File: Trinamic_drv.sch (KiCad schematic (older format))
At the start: 5 parts

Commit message: Added FET Drivers + PNs. Started Trinamic drivers
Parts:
- added C? (x2): C, symbol Device:C
- added J? (x2): Conn_01x02, bountiful_harvest:MOLEX_1510481206_6.55p, symbol Connector_Generic:Conn_01x02
- added R? (x2): R, symbol Device:R
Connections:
- net labels added: +VDC, GND
- net labels removed: +24V
- wire segments 13 -> 37
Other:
- note added: "CLOSE TO PIN 31 AND 16"
- moved on the sheet: C?, U?

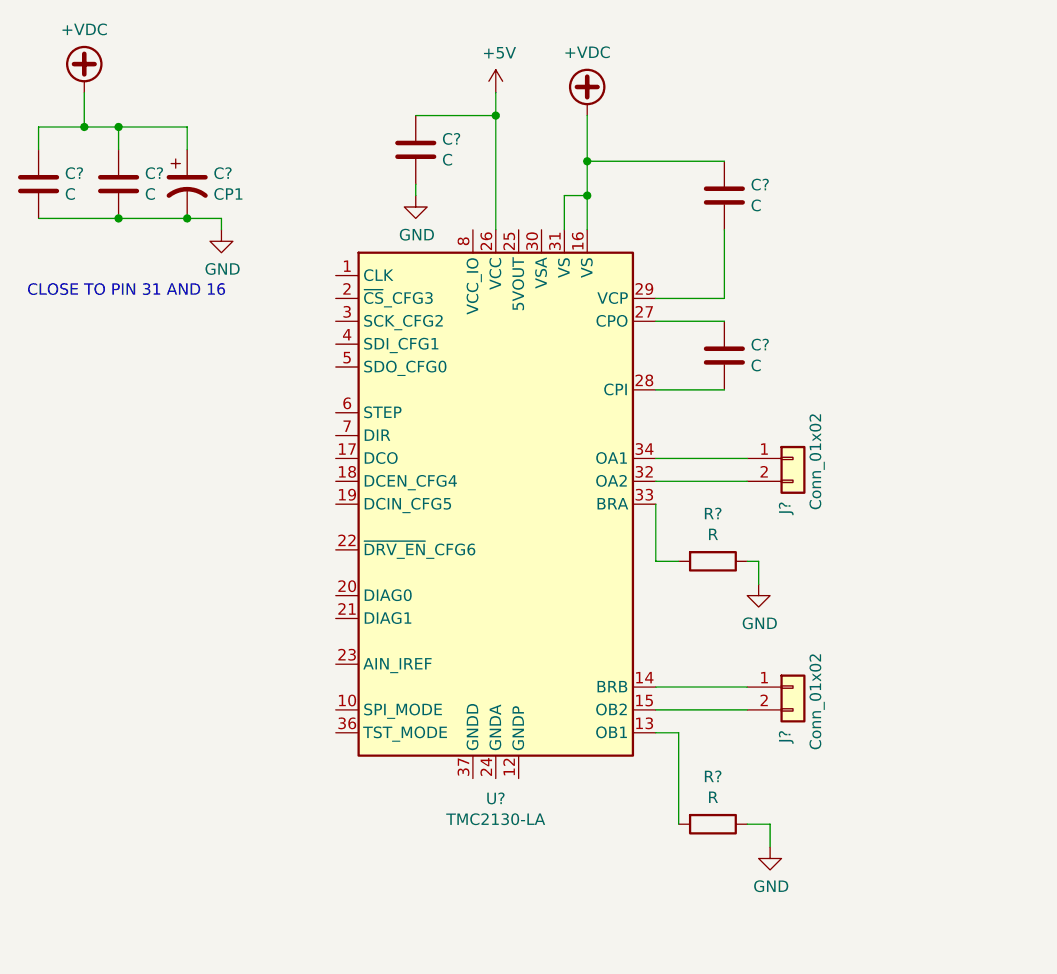
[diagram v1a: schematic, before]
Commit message: added SPI and sense resistors to stepper driver
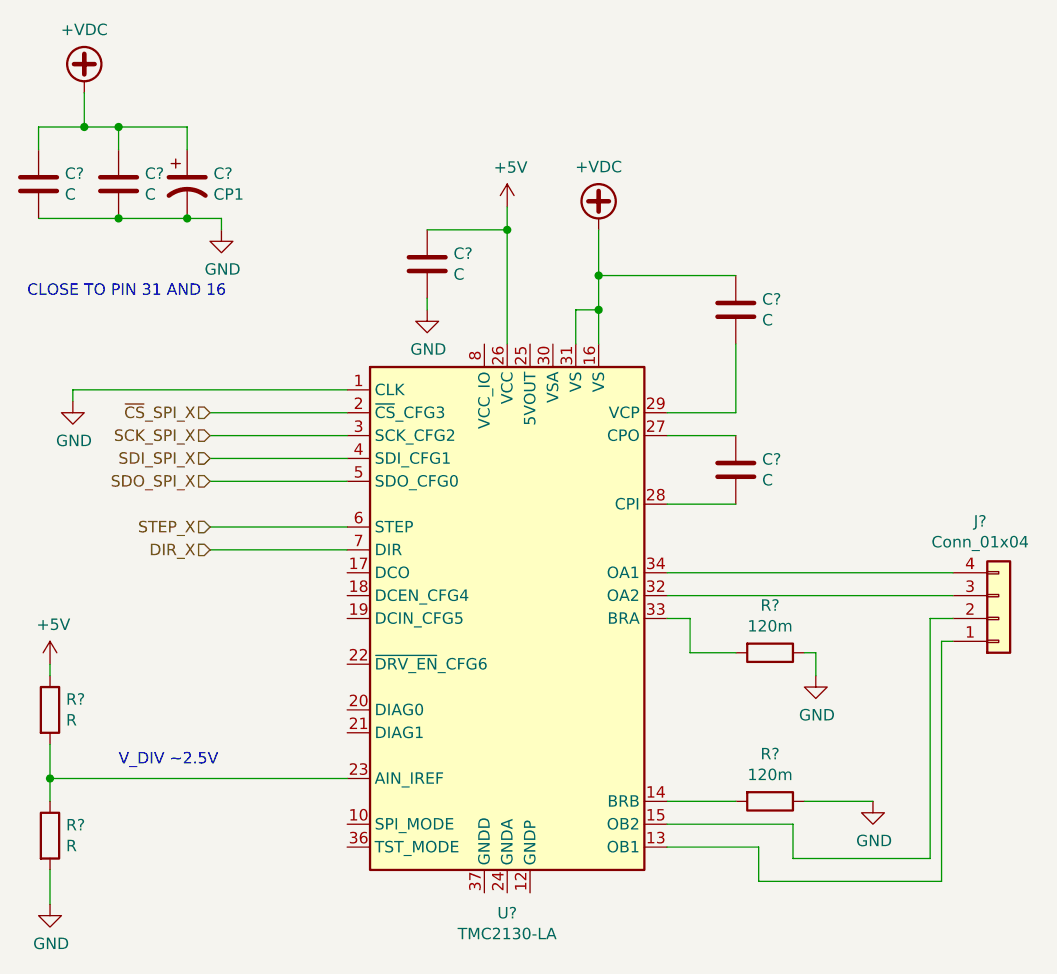
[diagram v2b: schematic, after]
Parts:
- removed J? (x2): Conn_01x02, bountiful_harvest:MOLEX_1510481206_6.55p, symbol Connector_Generic:Conn_01x02
- removed R?: R, symbol Device:R
- added J?: Conn_01x04, symbol Connector_Generic:Conn_01x04
- added R? (x2): R, symbol Device:R
- added R?: 120m, Resistors_SMD:R_2512_HandSoldering, symbol Device:R
- R?: value R -> 120m; footprint (none) -> Resistors_SMD:R_2512_HandSoldering; Manufacturer (none) -> Yageo; Vendor (none) -> Digi-Key; Vendor P/N (none) -> 311-0.12TCT-ND
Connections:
- net +5V: now also R?.1
- net GND: now also U?.1 (CLK), R?.1, R?.2
- net at U?.13 (OB1): now also J?.1 (Pin_1)
- net at U?.14 (BRB): now also R?.2
- net at U?.15 (OB2): now also J?.2 (Pin_2)
- net ~CS~_SPI_X: now reaches U?.2 (~CS~_CFG3)
- net at U?.23 (AIN_IREF): now also R?.1, R?.2
- net SCK_SPI_X: now reaches U?.3 (SCK_CFG2)
- net at U?.32 (OA2): now also J?.3 (Pin_3)
- net at U?.34 (OA1): now also J?.4 (Pin_4)
- net SDI_SPI_X: now reaches U?.4 (SDI_CFG1)
- net SDO_SPI_X: now reaches U?.5 (SDO_CFG0)
- net STEP_X: now reaches U?.6 (STEP)
- net DIR_X: now reaches U?.7 (DIR)
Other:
- note added: "V_DIV ~~2.5V"
- moved on the sheet: C?, R?, U?

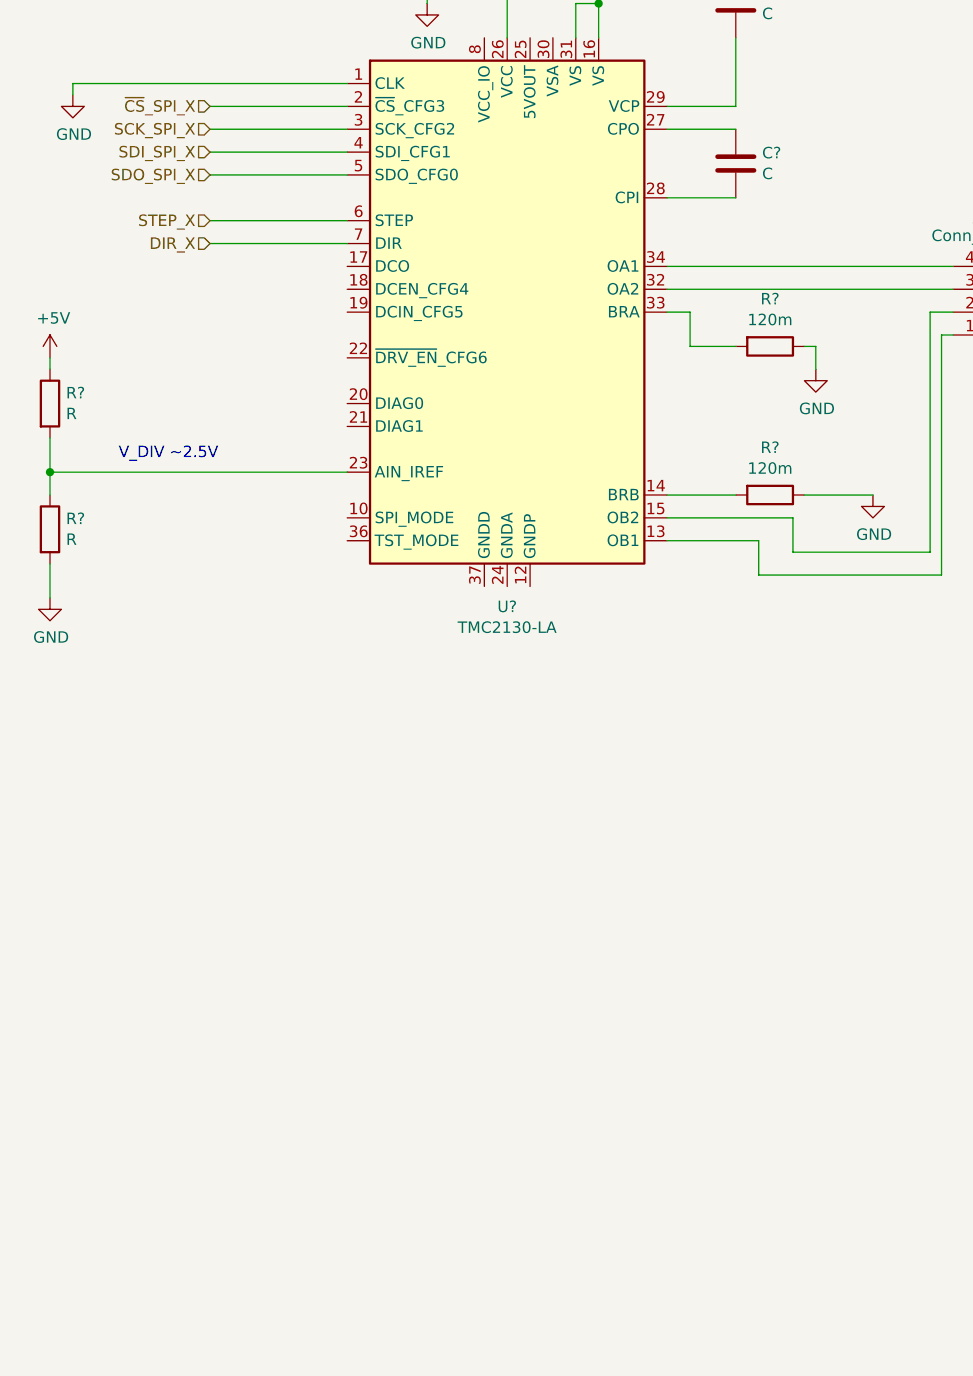
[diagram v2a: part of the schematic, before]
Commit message: Adding charge pump caps, SPI select, test mode
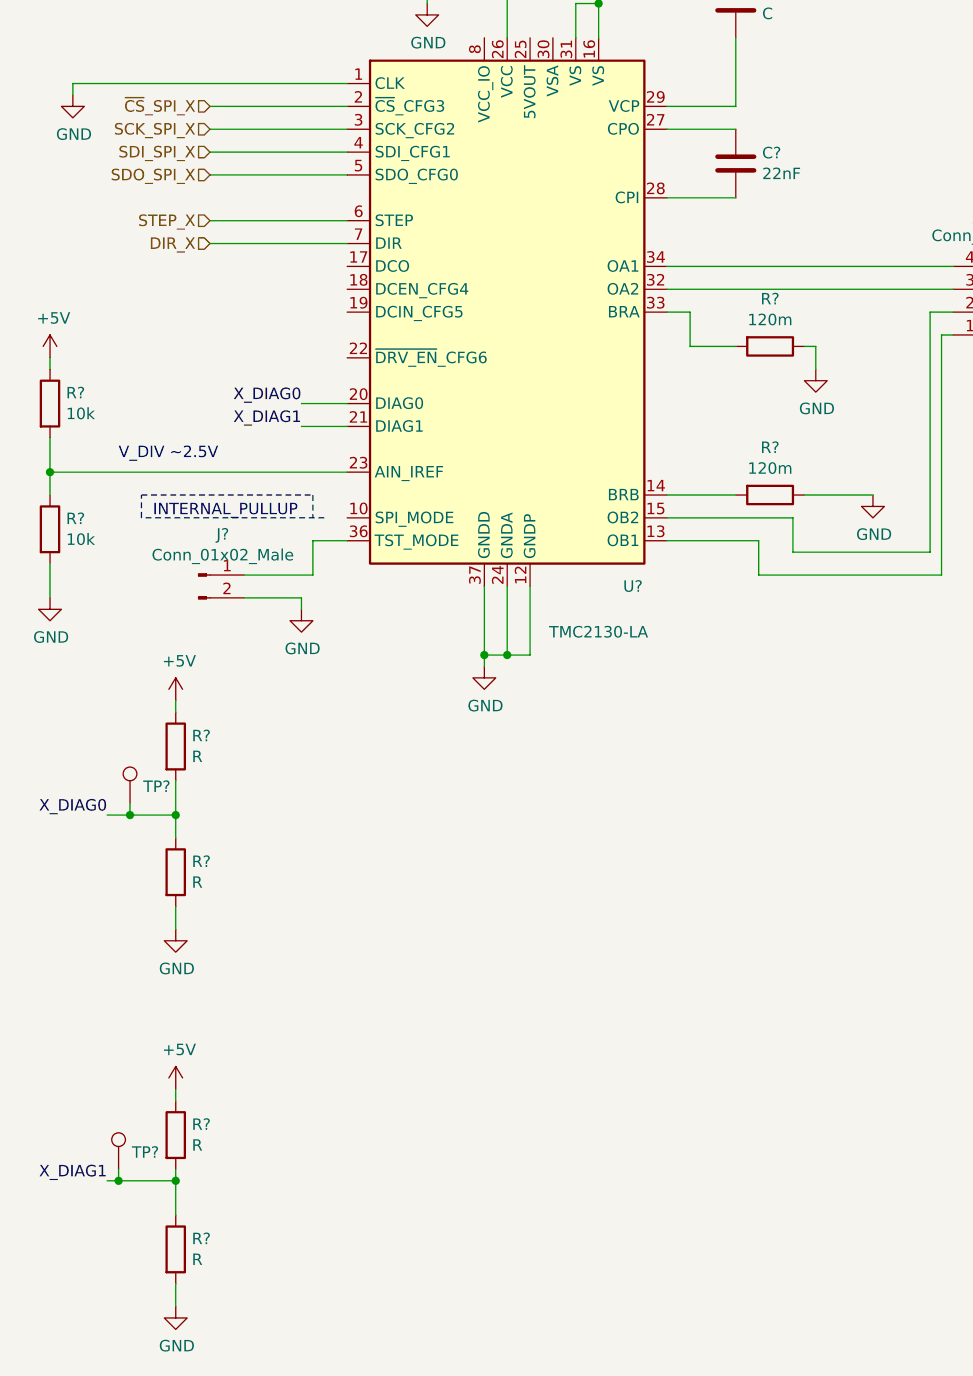
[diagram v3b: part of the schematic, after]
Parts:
- removed R? (x2): R, symbol Device:R
- added J?: Conn_01x02_Male, Pin_Headers:Pin_Header_Straight_1x02_Pitch2.54mm, symbol Connector:Conn_01x02_Male
- added R? (x2): 10k, Resistors_SMD:R_0603_HandSoldering, symbol Device:R
- added R? (x4): R, symbol Device:R
- added TP? (x2): TestPoint, Measurement_Points:Test_Point_Keystone_5000-5004_Miniature, symbol Connector:TestPoint
- C?: footprint (none) -> Capacitors_SMD:C_0805_HandSoldering; Vendor (none) -> Digi-Key; Vendor P/N (none) -> 1276-6557-1-ND
- C?: value C -> 22nF; footprint (none) -> Capacitors_SMD:C_0805_HandSoldering; Vendor (none) -> Digi-Key; Vendor P/N (none) -> 311-3176-1-ND
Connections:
- net +5V: now also R?.1, R?.1, R?.1
- net GND: now also U?.11 (GNDD), U?.12 (GNDP), U?.24 (GNDA), U?.35 (GNDP), U?.37 (GNDD), J?.2 (Pin_2), R?.2, R?.2, R?.2
- net X_DIAG0: now reaches U?.20 (DIAG0)
- net X_DIAG0: now also R?.1, R?.2, TP?.1
- net X_DIAG1: now reaches U?.21 (DIAG1)
- net X_DIAG1: now also R?.1, R?.2, TP?.1
- net at U?.23 (AIN_IREF): now also R?.1, R?.2
- net at U?.36 (TST_MODE): now also J?.1 (Pin_1)
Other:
- note added: "INTERNAL_PULLUP"

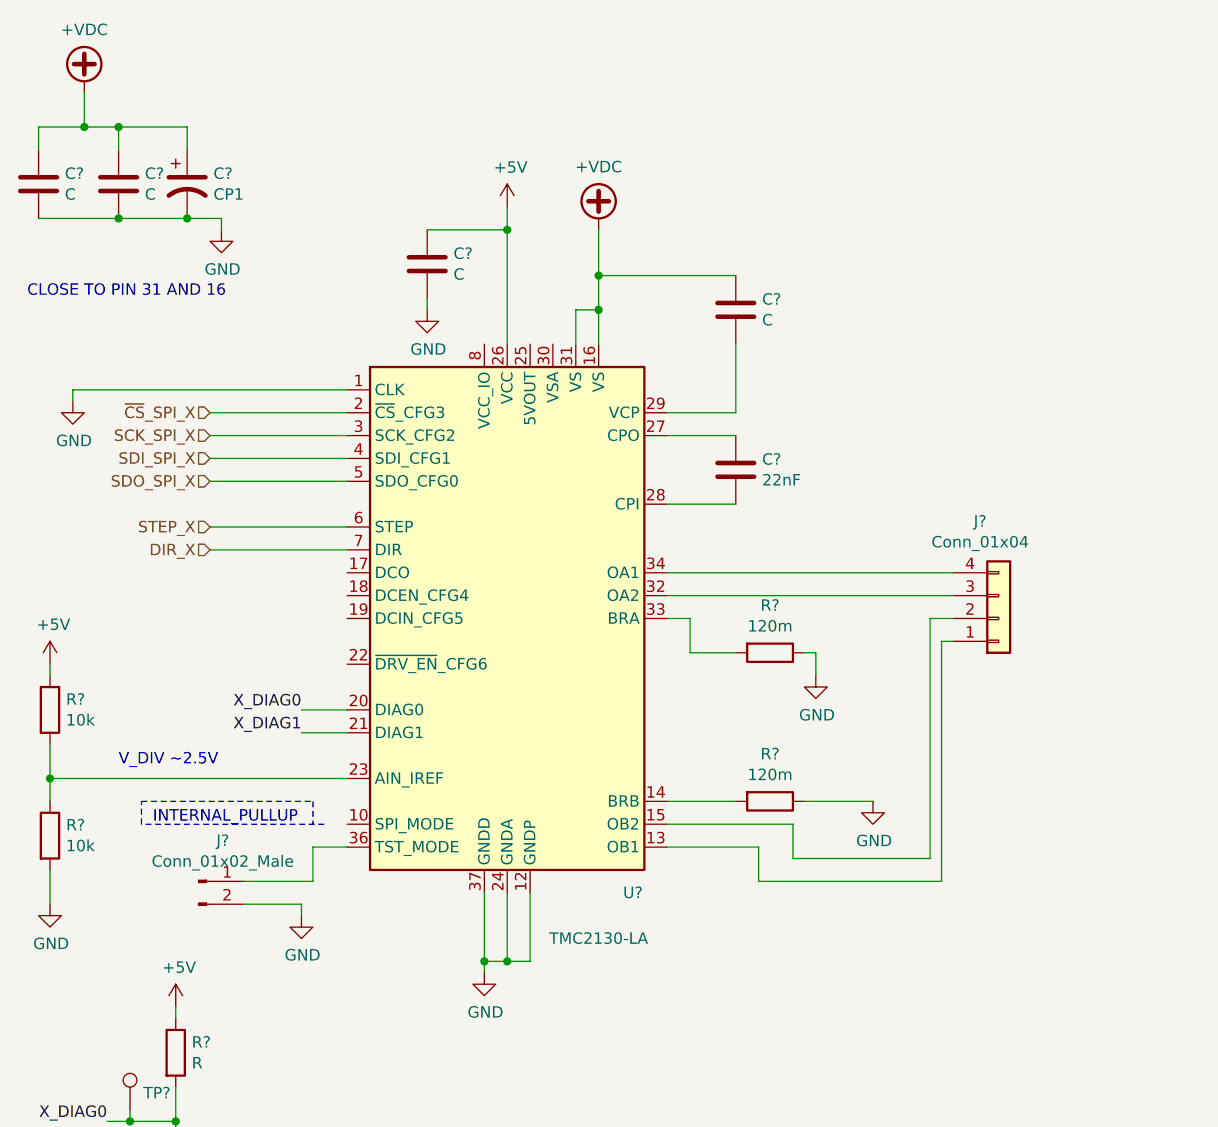
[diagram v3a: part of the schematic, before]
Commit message: Added Caps, finished pinout for dev stepper driver
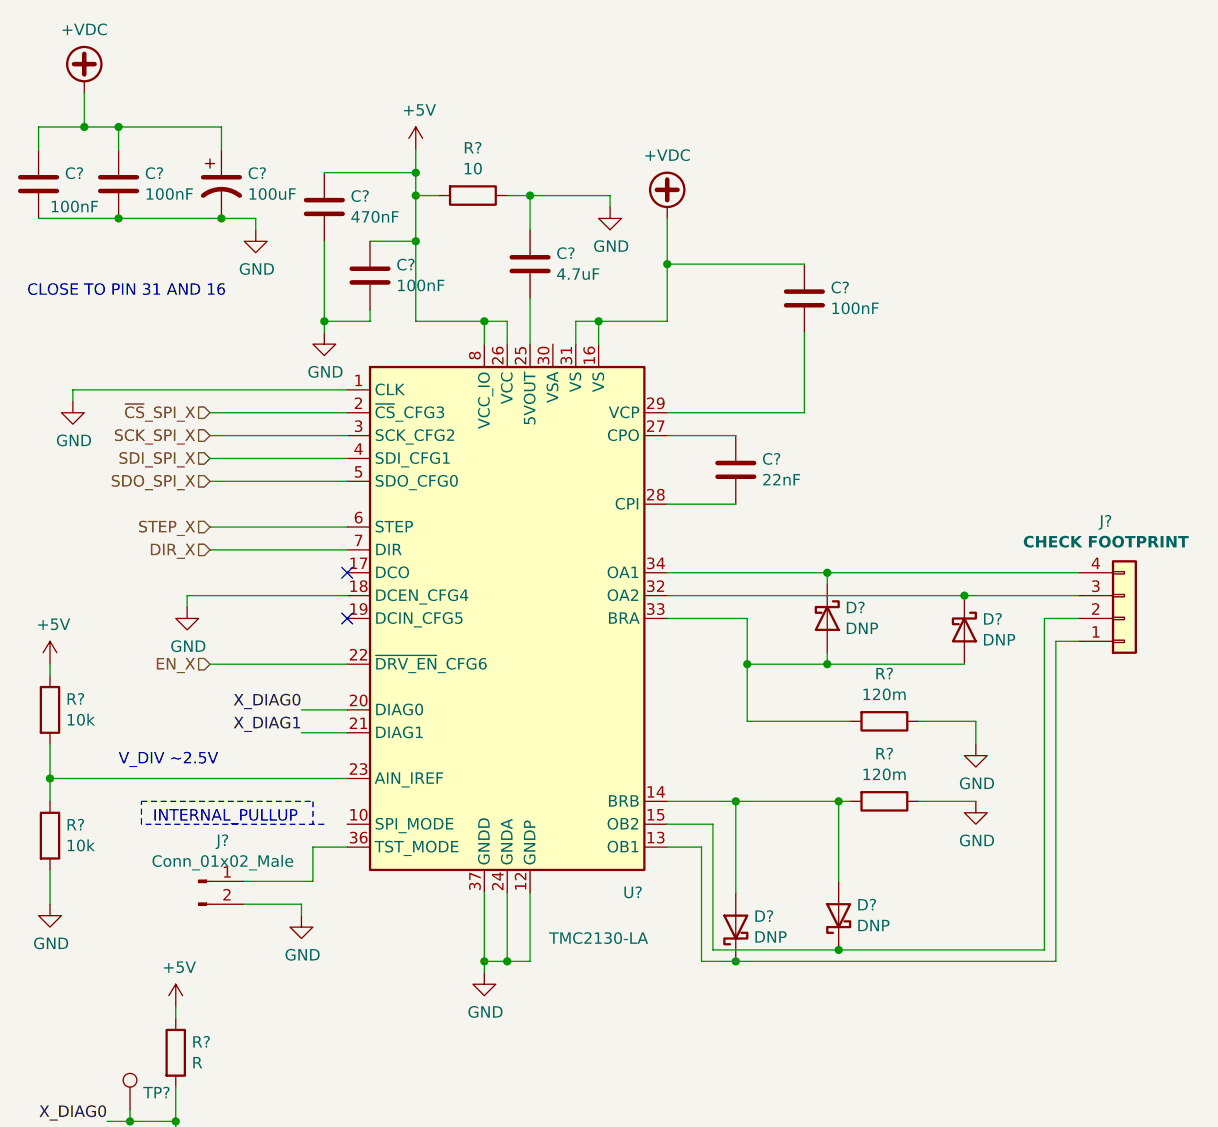
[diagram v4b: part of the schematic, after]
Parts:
- removed C? (x2): C, symbol Device:C
- added C?: 4.7uF, Capacitors_SMD:C_0805_HandSoldering, symbol Device:C
- added C? (x3): 100nF, Capacitors_SMD:C_0805_HandSoldering, symbol Device:C
- added D? (x4): DNP, Diodes_SMD:D_TUMD2, symbol Device:D_Schottky
- added R?: 10, symbol Device:R
- C?: value C -> 470nF; Manufacturer P/N (none) -> GCM21BR71H474KA55L; Vendor (none) -> Digi-Key; Vendor P/N (none) -> 490-4788-1-ND
- C?: value CP1 -> 100uF; footprint (none) -> Capacitors_SMD:CP_Elec_8x10; Vendor (none) -> Digi-Key; Vendor P/N (none) -> PCE4210CT-ND
- C?: value C -> 100nF
- J?: value Conn_01x04 -> CHECK FOOTPRINT; footprint (none) -> Connectors_Molex:Molex_KK-6410-04_04x2.54mm_Straight; Vendor P/N (none) -> WM4826-ND
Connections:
- net +5V: now also U?.8 (VCC_IO), C?.1, R?.2
- net +VDC: now also C?.1, C?.1
- net GND: now also U?.18 (DCEN_CFG4), C?.1, C?.2, C?.2, C?.2, R?.1
- net at J?.1 (Pin_1), U?.13 (OB1): now also D?.1 (K)
- net at R?.2, U?.14 (BRB): now also D?.2 (A), D?.2 (A)
- net at J?.2 (Pin_2), U?.15 (OB2): now also D?.1 (K)
- net EN_X: now reaches U?.22 (~DRV_EN~_CFG6)
- net at U?.25 (5VOUT): now also C?.2
- net at J?.3 (Pin_3), U?.32 (OA2): now also D?.1 (K)
- net at R?.2, U?.33 (BRA): now also D?.2 (A), D?.2 (A)
- net at J?.4 (Pin_4), U?.34 (OA1): now also D?.1 (K)
- no-connect marks 0 -> 2
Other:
- moved on the sheet: C?, J?, R?
